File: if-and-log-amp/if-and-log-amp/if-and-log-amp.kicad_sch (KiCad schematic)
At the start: 65 parts, among them J301 Conn_Coaxial, J306 Conn_Coaxial, SW301 Video, U301 AD603AQ, U302 L78L05_TO92, U303 LM317L_TO92, U304 AD8307AN, U305 CA3140

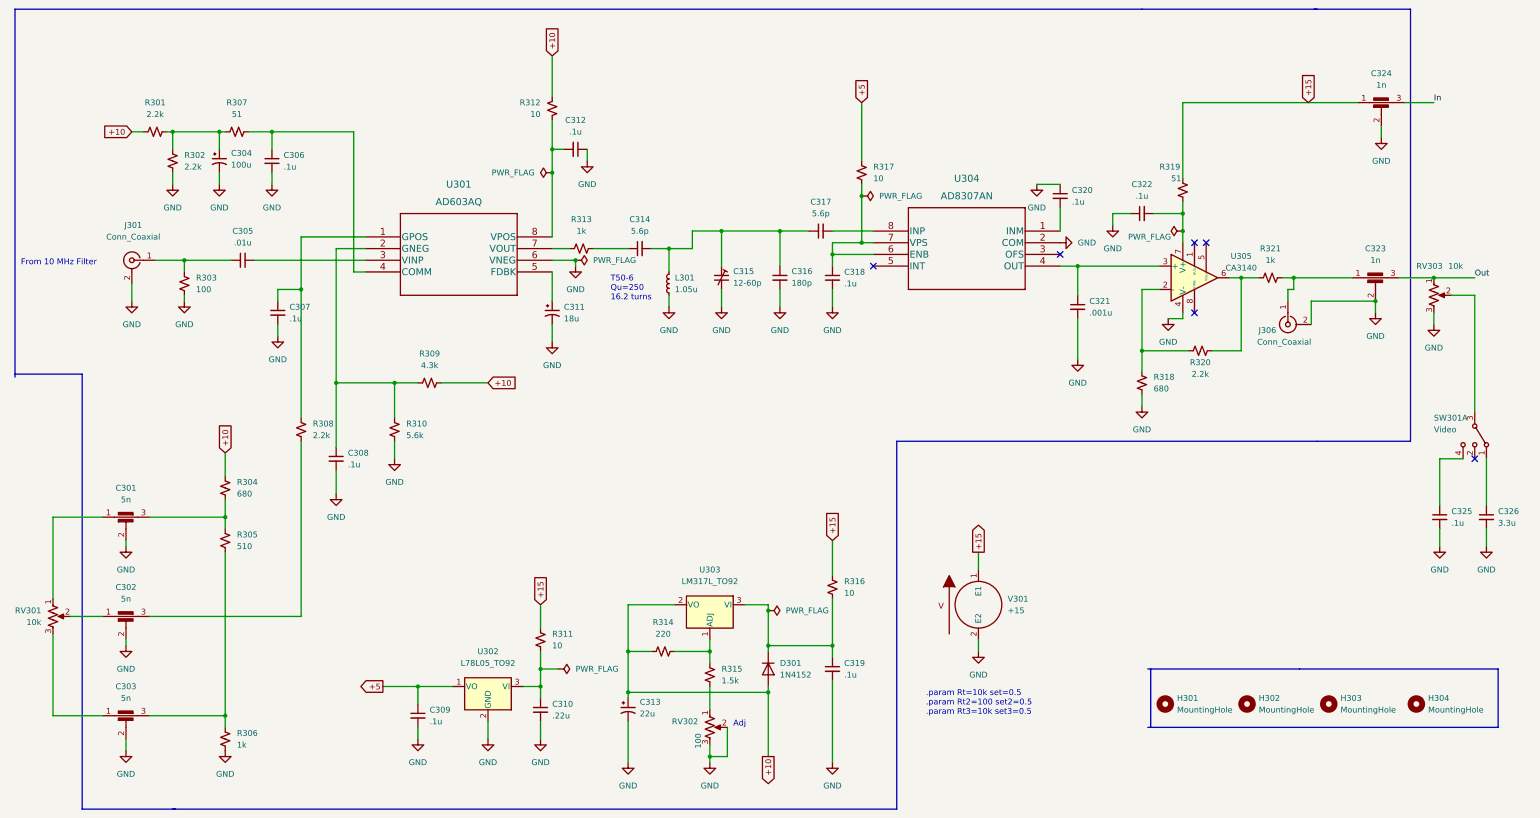
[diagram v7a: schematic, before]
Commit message: further improvements to if-log amp
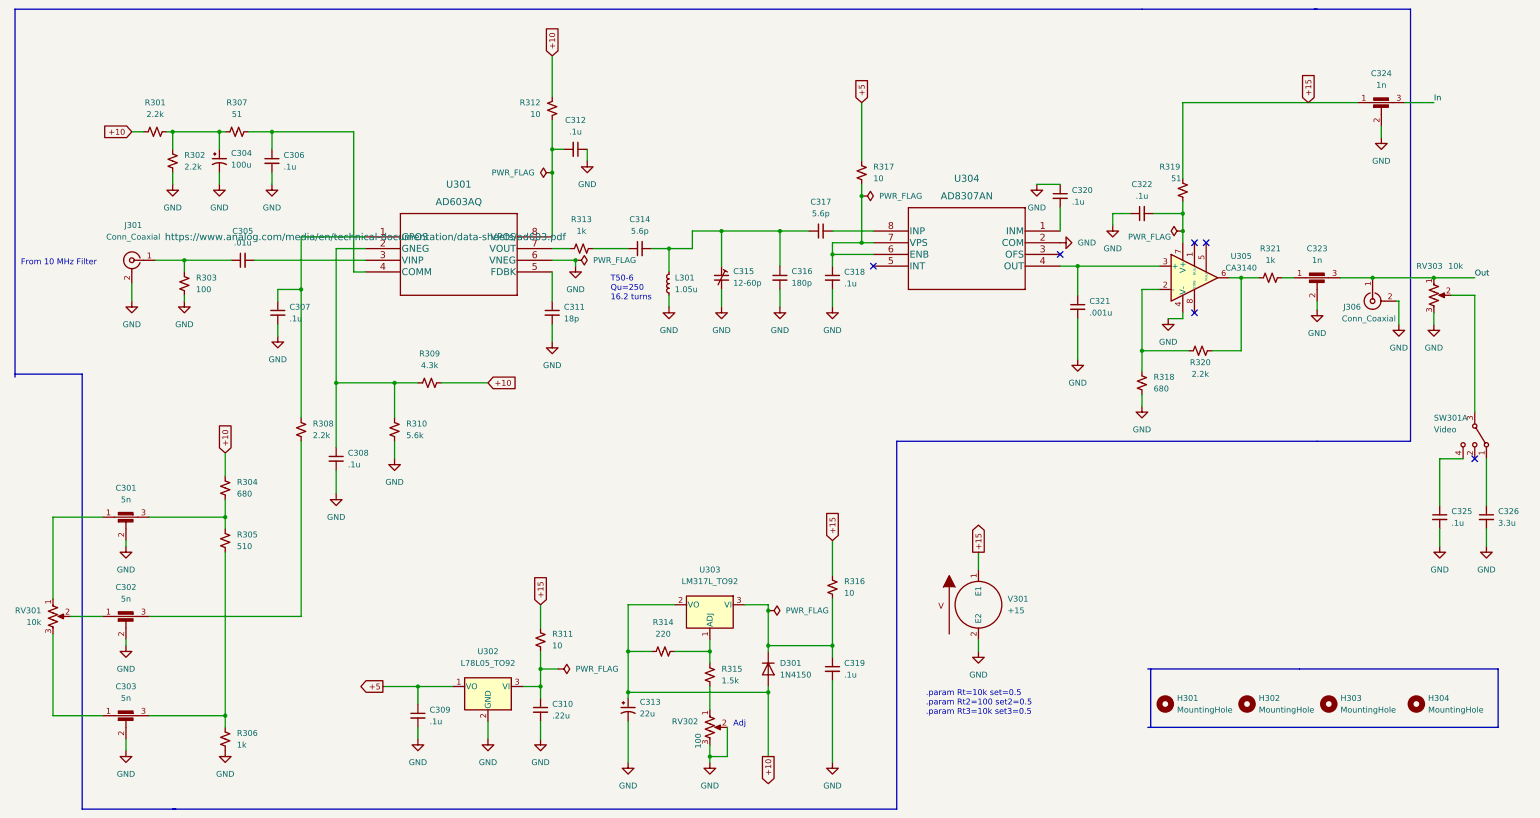
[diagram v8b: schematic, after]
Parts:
- C305, C306, C307, C308, C309, C310, C312, C314, C316, C317, C318, C319, C320, C321, C322: footprint Capacitor_THT:C_Radial_D4.0mm_H5.0mm_P1.50mm -> Capacitor_THT:CP_Radial_D5.0mm_P2.50mm
- C311: value 18u -> 18p; footprint Capacitor_THT:C_Radial_D4.0mm_H5.0mm_P1.50mm -> Capacitor_THT:CP_Radial_D5.0mm_P2.50mm; symbol Device:C_Polarized_Small_US -> Device:C_Small
- D301: value 1N4152 -> 1N4150; Spice_Node_Sequence (none) -> 2 1
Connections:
- net Out: now also J306.1 (In)
- net at C323.1, R321.2: no longer J306.1 (In)
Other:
- moved on the sheet: C323, J306
